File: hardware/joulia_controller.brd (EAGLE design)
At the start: 122.9 x 67.9 mm, 40 parts, among them IC1 LM2902D, IC2 LM2902D, U1 MMBT2222ALT1G, U2 MMBT2222ALT1G

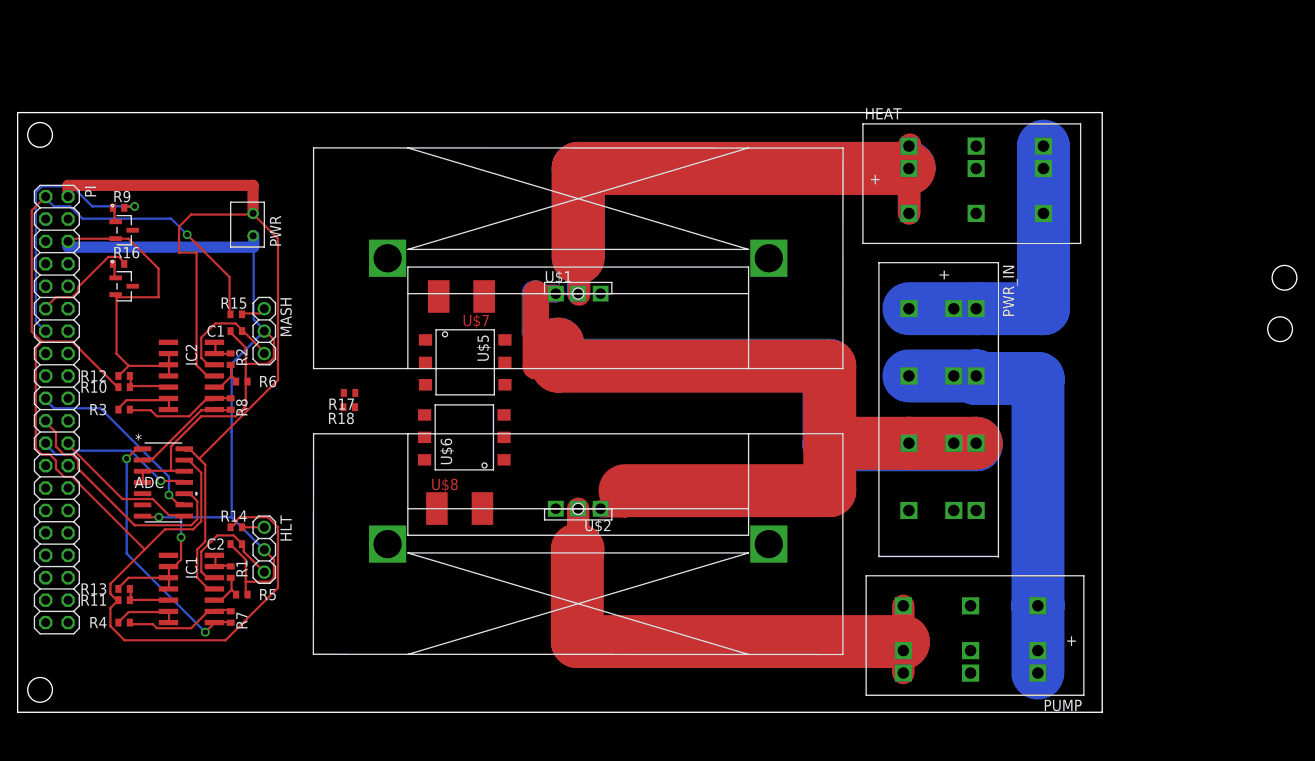
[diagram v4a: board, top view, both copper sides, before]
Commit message: Routing of smaller traces.
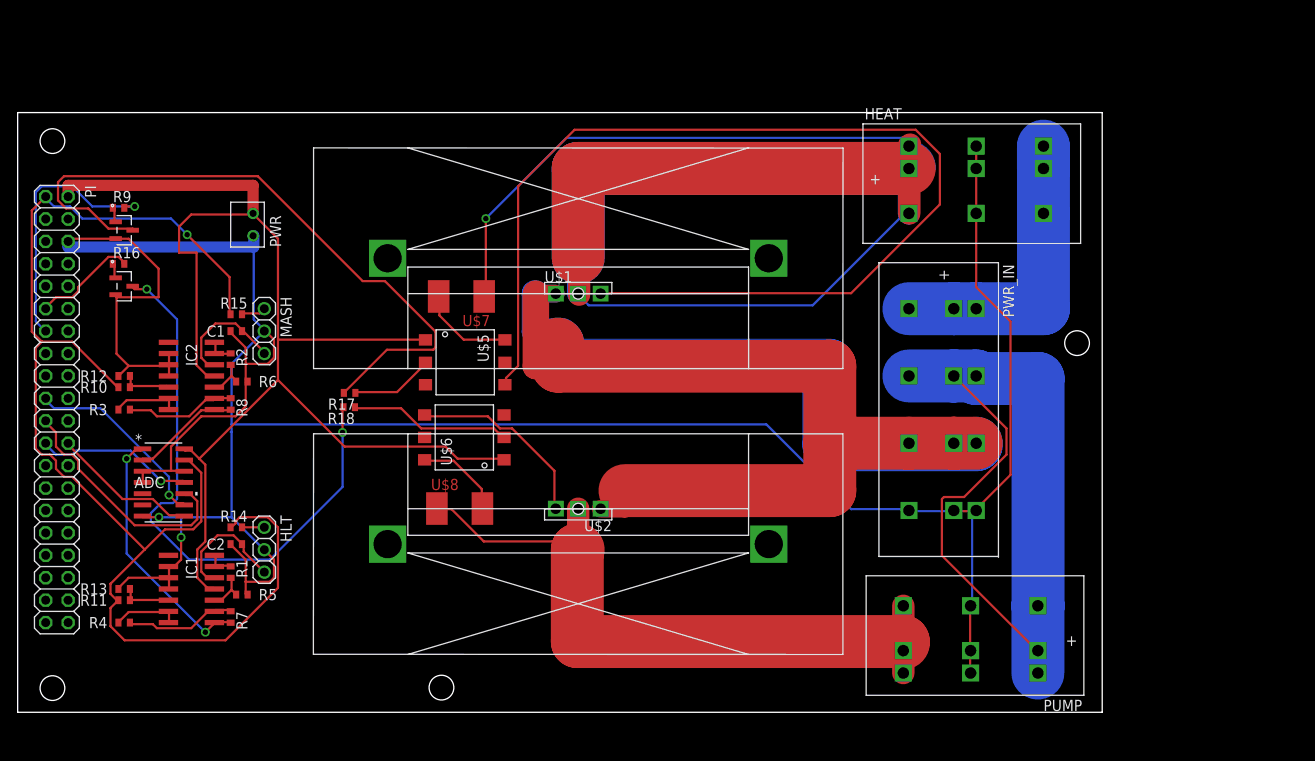
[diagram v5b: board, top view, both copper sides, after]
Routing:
- net GND: track 174.4 -> 326.6 mm
- net N$19: track 0.00 -> 123.0 mm
- net N$22: track 11.6 -> 114.9 mm, vias 0 -> 1
- net N$13: track 0.00 -> 76.7 mm
- net N$17: track 0.00 -> 67.5 mm, vias 0 -> 2
- net +5V: track 106.3 -> 152.4 mm
- net N$27: track 48.6 -> 93.4 mm
- net N$23: track 0.00 -> 21.7 mm
- net N$24: track 63.7 -> 82.1 mm
- net N$18: track 0.00 -> 18.5 mm
- net N$20: track 0.00 -> 10.7 mm
- net N$21: track 0.00 -> 10.1 mm
- net N$14: track 0.00 -> 9.45 mm
- net N$25: track 41.1 -> 36.5 mm

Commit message: Fix optoisolator resistors and update power header
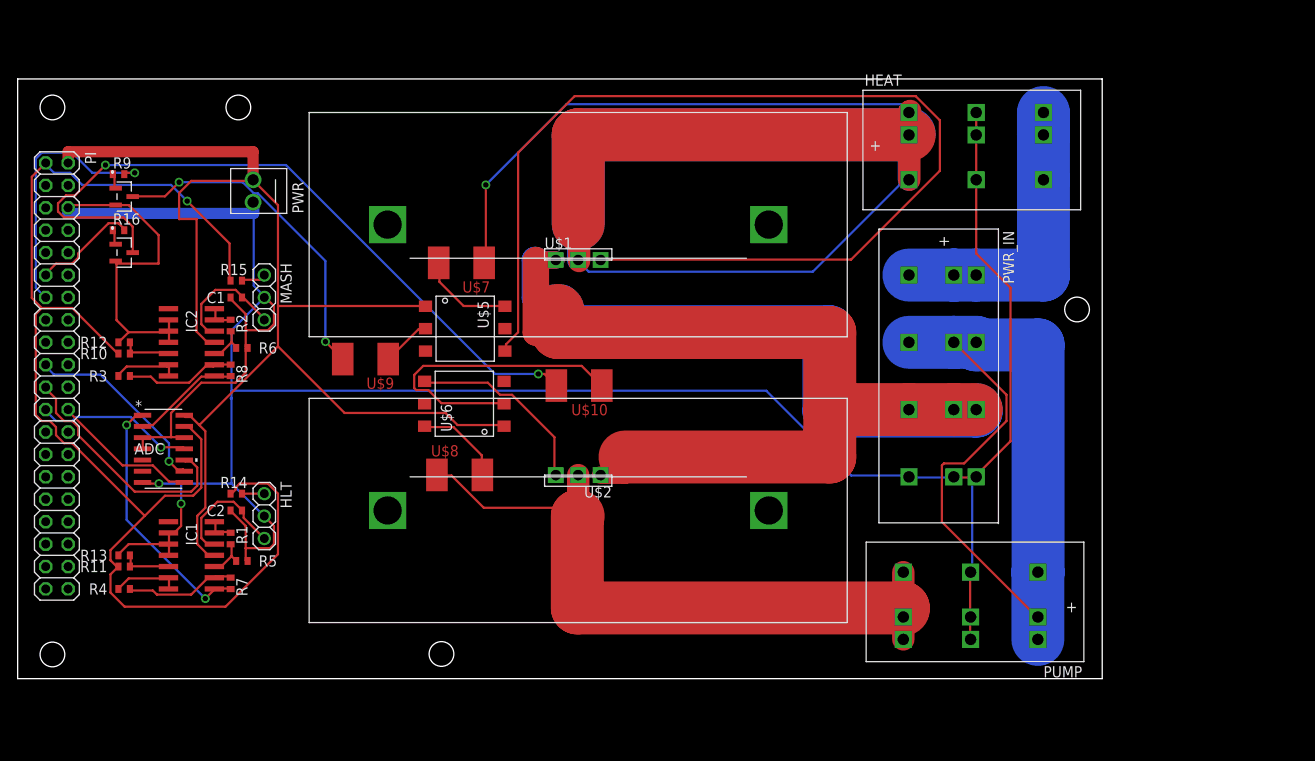
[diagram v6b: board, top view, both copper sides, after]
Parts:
- removed R17, R18: 220, resistor:R0402
- added U$10, U$9: CRM2512, digikey:2512(6432METRIC)
- moved C1 3.81 mm to (24.8, 43.2)
- moved HEAT 3.81 mm to (108.6, 64.1)
- moved IC2 3.81 mm to (19.7, 38.1)
- moved MASH 3.81 mm to (27.9, 43.2)
- moved PWR_IN 3.81 mm to (108.6, 38.1)
- moved R12 3.81 mm to (12.1, 38.1)
- moved R15 3.81 mm to (24.8, 45.1)
- moved R2 3.81 mm to (24.1, 40.0)
- moved R6 3.81 mm to (25.4, 37.5)
- moved U$3 3.81 mm to (63.5, 51.4)
- moved U$5 3.81 mm to (50.7, 39.6)
- moved U$6 3.81 mm to (50.6, 31.1)
- moved U1 3.81 mm to (12.1, 54.6)
- moved C2 3.81 mm to (24.8, 19.1)
- moved IC1 3.81 mm to (19.7, 14.0)
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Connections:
- net N$13: now also U$9.P$1; no longer R17.2
- net N$14: now also U$9.P$2; no longer R17.1
- net N$17: now also U$10.P$2, U$6.P$5; no longer R18.2, U2.3
- net N$18: now also U$10.P$1, U2.3; no longer R18.1, U$6.P$5
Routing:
- net N$18: track 18.5 -> 81.6 mm, vias 0 -> 2
- net N$13: track 76.7 -> 38.1 mm, vias 0 -> 2
- net N$17: track 67.5 -> 35.0 mm, vias 2 -> 0
- net N$14: track 9.45 -> 5.68 mm

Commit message: Improves board layout and autorouting
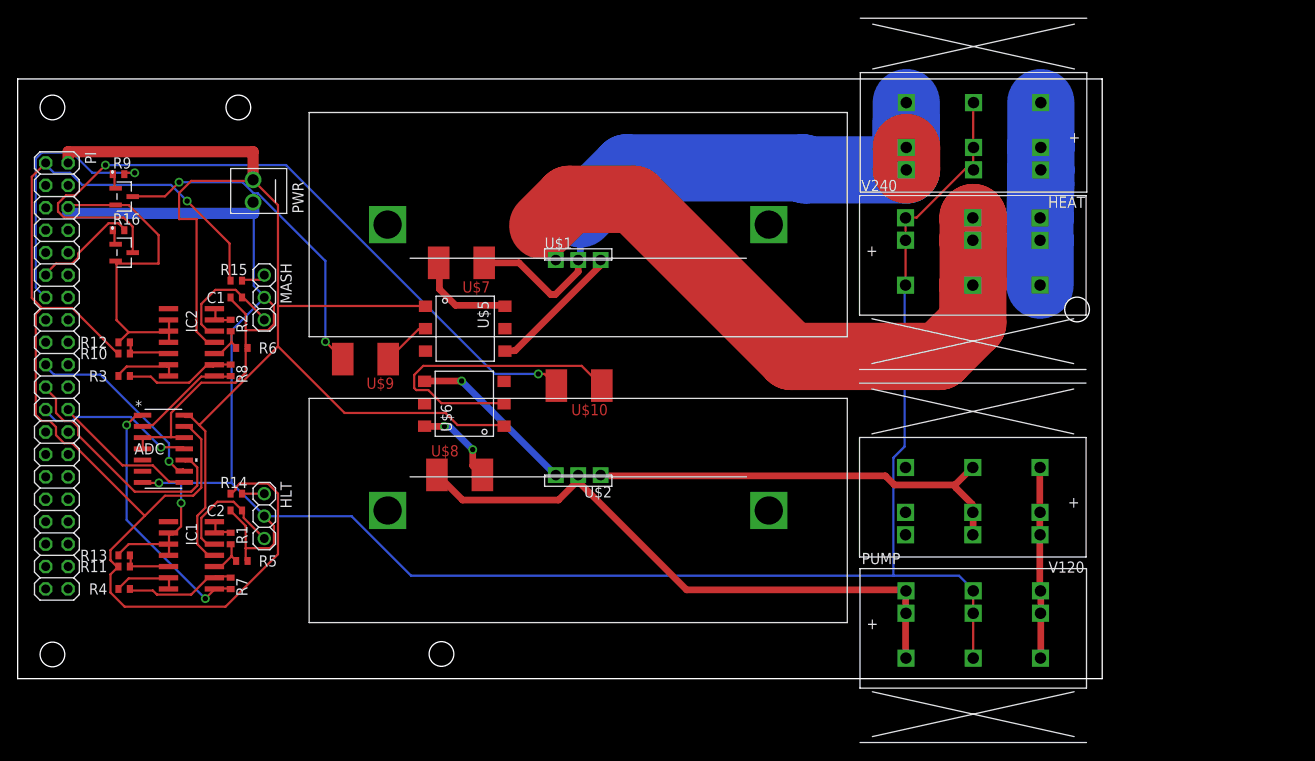
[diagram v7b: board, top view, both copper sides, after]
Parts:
- removed PWR_IN: PC1720592, digikey:PC-PCV5/4-G-7.62
- added V120, V240: PC1720589, digikey:PC-PCV5/3-G-7.62
- moved HEAT 6.51 mm to (108.3, 57.6), turned to 180 degrees
- moved PUMP 5.51 mm to (108.2, 9.95), turned to 0 degrees
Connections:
- removed net N$25: HEAT.P$4, HEAT.P$5, HEAT.P$6, PWR_IN.P$7, PWR_IN.P$8, PWR_IN.P$9
- new net N$29: HEAT.P$7, HEAT.P$8, HEAT.P$9, V240.P$4, V240.P$5, V240.P$6
- new net N$32: U$1.A1, V240.P$1, V240.P$2, V240.P$3
- net GND: now also V240.P$7, V240.P$8, V240.P$9; no longer PWR_IN.P$10, PWR_IN.P$11, PWR_IN.P$12
- net N$22: now also HEAT.P$4, HEAT.P$5, HEAT.P$6; no longer HEAT.P$7, HEAT.P$8, HEAT.P$9
- net N$24: now also PUMP.P$7, PUMP.P$8, PUMP.P$9; no longer PUMP.P$4, PUMP.P$5, PUMP.P$6
- net N$26: now also V120.P$1, V120.P$2, V120.P$3; no longer PWR_IN.P$4, PWR_IN.P$5, PWR_IN.P$6, U$1.A1
- net N$27: now also PUMP.P$4, PUMP.P$5, PUMP.P$6, V120.P$7, V120.P$8, V120.P$9; no longer PUMP.P$7, PUMP.P$8, PUMP.P$9, PWR_IN.P$1, PWR_IN.P$2, PWR_IN.P$3
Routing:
- net N$26: track 177.8 -> 49.9 mm
- net N$19: track 123.0 -> 15.5 mm
- net N$32: track 0.00 -> 75.5 mm
- net N$27: track 93.4 -> 21.7 mm
- net N$28: track 47.6 -> 0.00 mm
- net N$30: track 47.6 -> 0.00 mm
- net N$22: track 114.9 -> 74.7 mm, vias 1 -> 0
- net N$25: track 36.5 -> 0.00 mm
- net N$29: track 3.80 -> 20.8 mm
- net N$24: track 82.1 -> 69.4 mm
- net N$31: track 7.84 -> 0.00 mm
- net N$23: track 21.7 -> 19.7 mm, vias 0 -> 1
- net GND: track 326.6 -> 325.1 mm
- net N$20: track 10.7 -> 11.3 mm
- net N$21: track 10.1 -> 9.89 mm, vias 0 -> 2

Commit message: Using smaller resistor for optoisolator emitter.
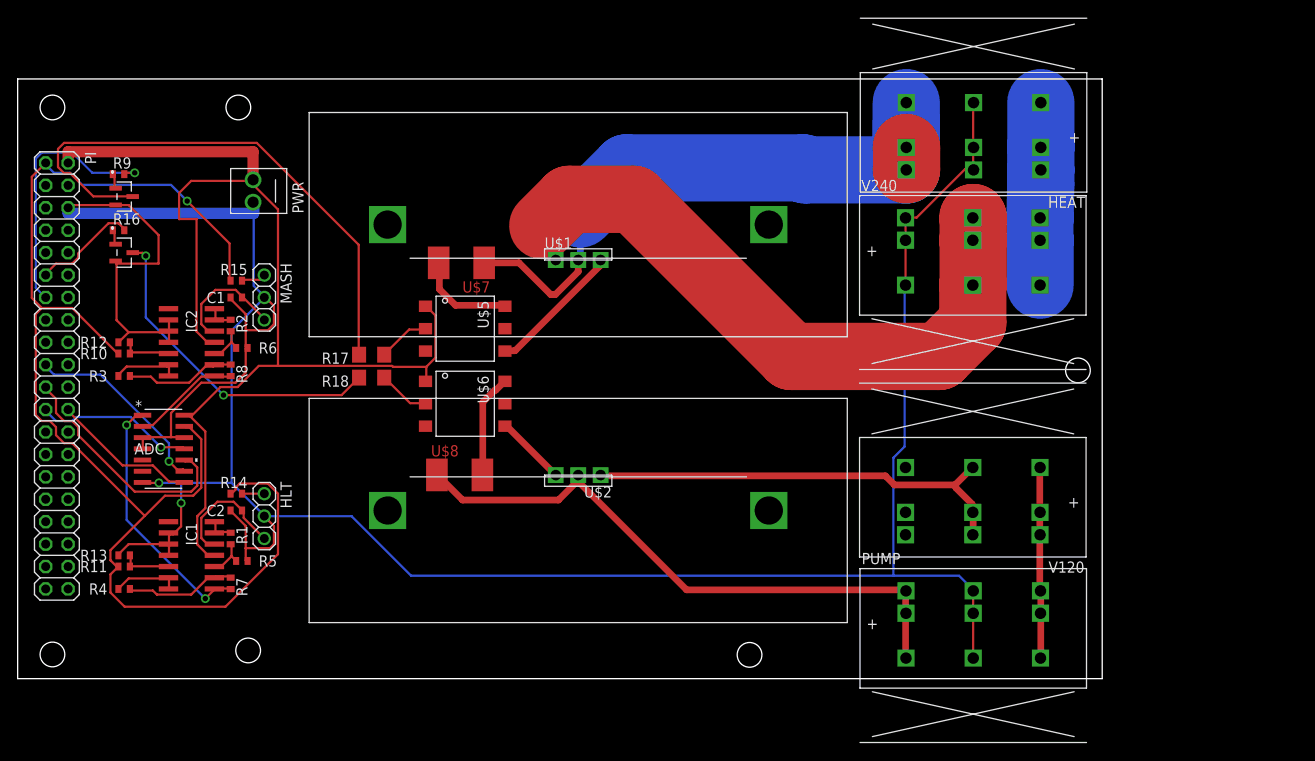
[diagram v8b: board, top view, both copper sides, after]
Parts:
- removed U$10, U$9: CRM2512, digikey:2512(6432METRIC)
- added R17, R18: 330, resistor:R1206
- moved U$6 0.10 mm to (50.7, 31.1), turned to 270 degrees
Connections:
- net N$13: now also R17.1; no longer U$9.P$1
- net N$14: now also R17.2; no longer U$9.P$2
- net N$17: now also R18.2; no longer U$10.P$2
- net N$18: now also R18.1; no longer U$10.P$1
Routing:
- net N$18: track 81.6 -> 37.3 mm
- net N$17: track 35.0 -> 5.92 mm
- net N$13: track 38.1 -> 63.5 mm, vias 2 -> 0
- net +5V: track 152.4 -> 135.2 mm
- net N$23: track 19.7 -> 8.06 mm, vias 1 -> 0
- net N$21: track 9.89 -> 11.8 mm, vias 2 -> 0
